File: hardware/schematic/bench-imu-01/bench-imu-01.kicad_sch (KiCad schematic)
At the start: 23 parts, among them J1 USB4105-GH-A, J2 UART, J3 SWD, SW1 SW_PUSH, U1 STM32G031K8T6, U2 BMI270, U3 TLV75533PDBV, U4 USBLC6-2SC6

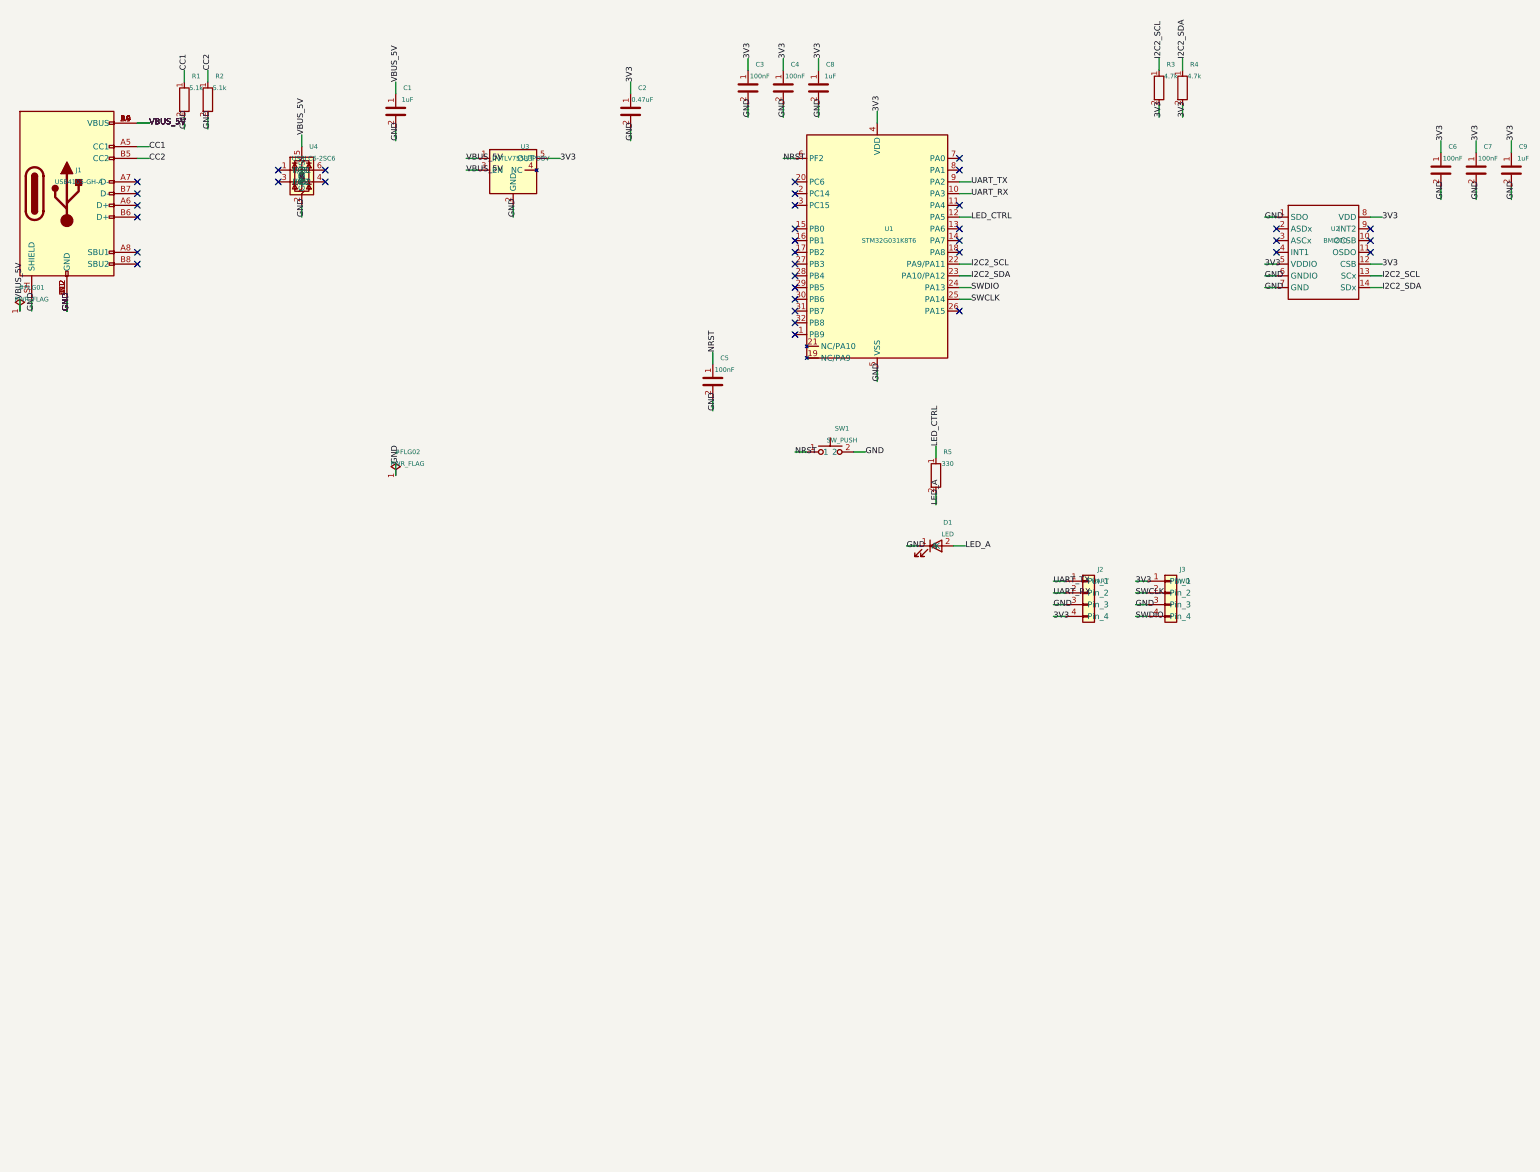
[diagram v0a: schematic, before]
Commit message: PCB Engineer: extend KiCad schematic to Rev 3-5 motor subsystem
The real KiCad project only ever captured Rev 2 (corrected) -- the
Motor Driver + Reaction Wheel subsystem (bench-imu-01-design.md section
7.5, already human-approved via bom/component-selection.md) was fully
designed but never transcribed into the actual .kicad_sch. Extends
generate_schematic.py (the project's own established authoring method)
to add all 25 new symbols: U5 (DRV10983, custom symbol, 24-pin HTSSOP,
pins independently re-verified against TI's real primary datasheet this
session), U6 (TPS26631PWPR, real library symbol+footprint), J4 (Same Sky
PJ-102AH barrel jack), D2/D3 (protection diodes), F1 (PTC fuse, custom
footprint -- no library match exists), R6-R15, C10-C17, and a new 3-pin
interconnect for M1 (motor is off-board; design doc section 10 itself
left this connector choice unresolved).

Every net wired exactly per the design doc's own net-by-net table
(re-derived into real distinct electrical nets, since that table
describes signal paths through series elements, not flat net
membership). Footprint decisions (CONFIRMED vs. ASSUMPTION, with
reasoning) recorded in hardware/schematic/bench-imu-01/README.md,
including a real power-rating-driven choice (R9 = 1206, not 0603, for
its stated 1/4W rating) and a disclosed, low-blast-radius open item
(J4's exact sleeve/switch/tip pin mapping -- primary datasheet diagram
not renderable by available tooling; D2's series reverse-polarity
protection fails safe if wrong).

Verified via kicad-cli sch erc + sch export netlist + sch export bom
(the established workaround for the broken kicad-* MCP tools, re-verified
still broken this session): 48 real components, zero ERC errors, 2
disclosed non-blocking warnings (one pre-existing from Rev 2, one new
metadata-completeness-only finding on U1 pin 19/PA9 -- kiutils 1.4.8
doesn't expose KiCad's per-instance 'alternate pin function' feature;
the wiring itself is electrically correct, independently re-confirme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
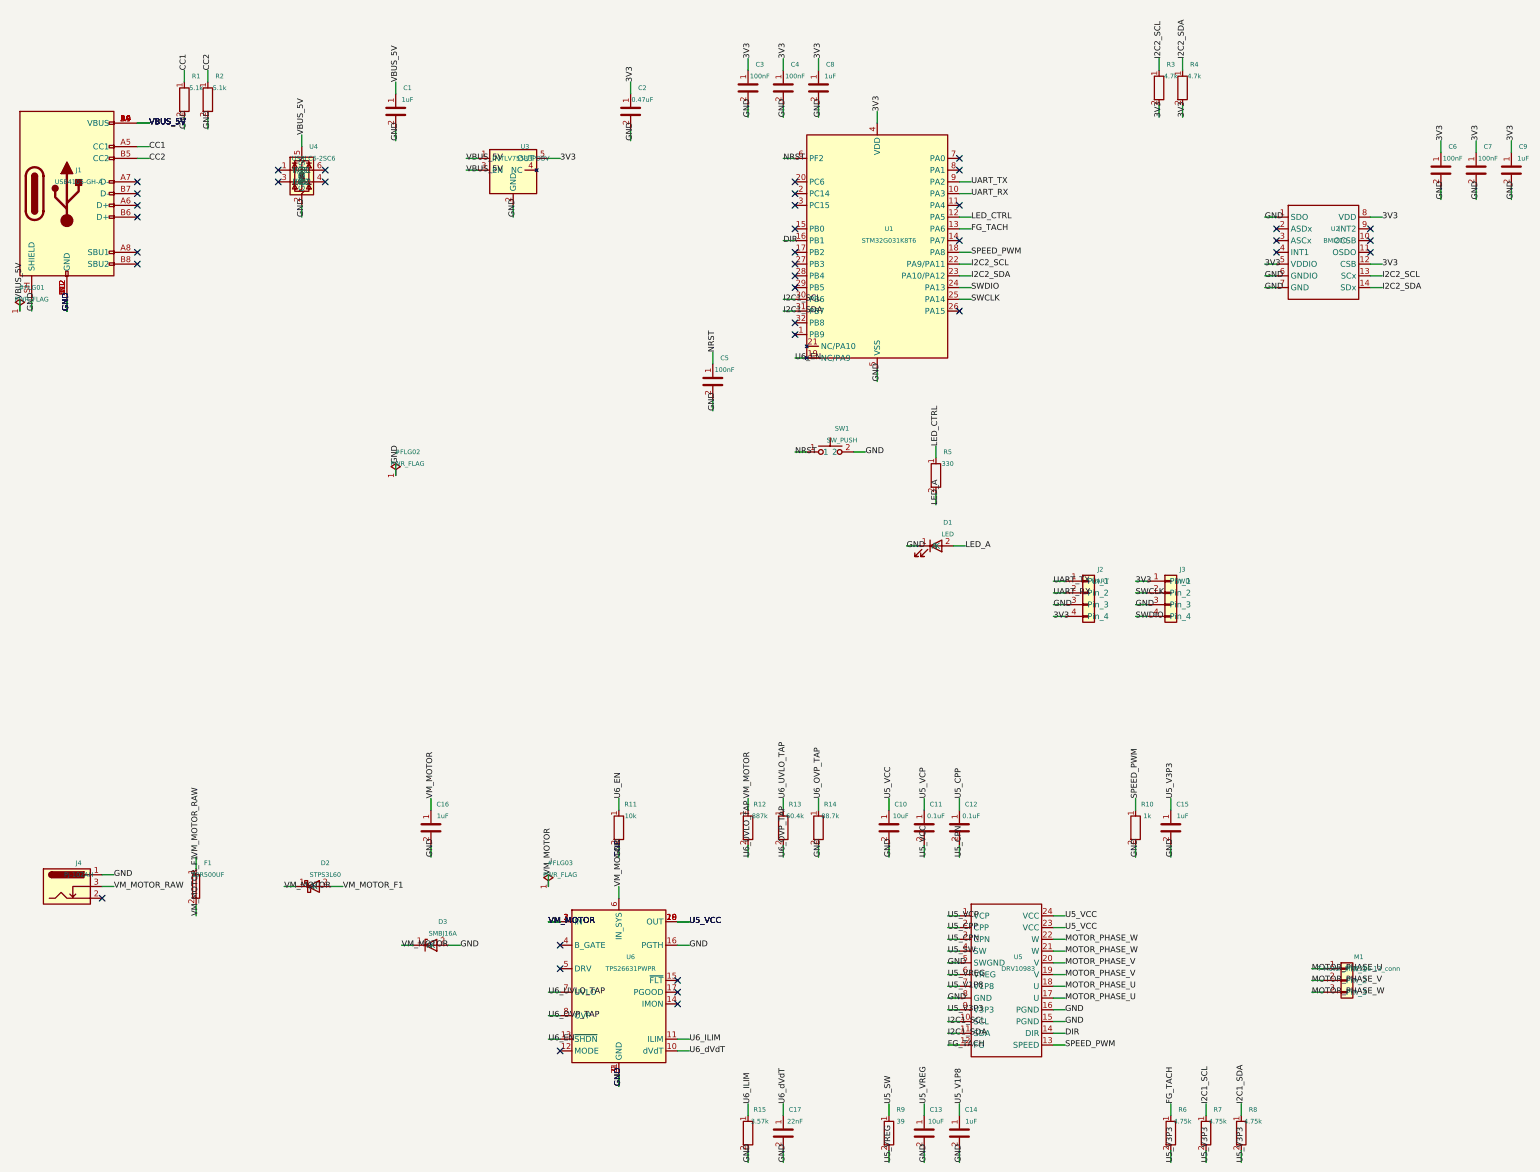
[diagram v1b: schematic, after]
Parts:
- added C10, C13: 10uF, Capacitor_SMD:C_0805_2012Metric, symbol Device:C
- added C11, C12: 0.1uF, Capacitor_SMD:C_0603_1608Metric, symbol Device:C
- added C14, C15, C16: 1uF, Capacitor_SMD:C_0603_1608Metric, symbol Device:C
- added C17: 22nF, Capacitor_SMD:C_0603_1608Metric, symbol Device:C
- added D2: STPS3L60, Diode_SMD:D_SMB, symbol Device:D_Schottky
- added D3: SMBJ16A, Diode_SMD:D_SMB, symbol Device:D_Zener
- added F1: 30R500UF, bench-imu-01:Fuse_Littelfuse_30R500UF_Radial_D14.0mm_P10.2mm, symbol Device:Fuse
- added J4: PJ-102AH, Connector_BarrelJack:BarrelJack_CUI_PJ-102AH_Horizontal, symbol Connector:Barrel_Jack_Switch
- added M1: T-Motor_MN2206-13_conn, TerminalBlock:TerminalBlock_MaiXu_MX126-5.0-03P_1x03_P5.00mm, symbol Connector_Generic:Conn_01x03
- added R10: 1k, Resistor_SMD:R_0603_1608Metric, symbol Device:R
- added R11: 10k, Resistor_SMD:R_0603_1608Metric, symbol Device:R
- added R12: 887k, Resistor_SMD:R_0603_1608Metric, symbol Device:R
- added R13: 60.4k, Resistor_SMD:R_0603_1608Metric, symbol Device:R
- added R14: 88.7k, Resistor_SMD:R_0603_1608Metric, symbol Device:R
- added R15: 3.57k, Resistor_SMD:R_0603_1608Metric, symbol Device:R
- added R6, R7, R8: 4.75k, Resistor_SMD:R_0603_1608Metric, symbol Device:R
- added R9: 39, Resistor_SMD:R_1206_3216Metric, symbol Device:R
- added U5: DRV10983, Package_SO:HTSSOP-24-1EP_4.4x7.8mm_P0.65mm_EP3.2x5mm, symbol bench-imu-01:DRV10983
- added U6: TPS26631PWPR, Package_SO:HTSSOP-20-1EP_4.4x6.5mm_P0.65mm_EP3.4x6.5mm_Mask2.96x2.96mm_ThermalVias, symbol Power_Management:TPS26631PWP
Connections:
- net GND: now also C10.2, C13.2, C14.2, C15.2, C16.2, C17.2, D3.2 (A), J4.1, R10.2, R11.2, R14.2, R15.2, U5.15 (PGND), U5.16 (PGND), U5.5 (SWGND), U5.8 (GND), U6.16 (PGTH), U6.21 (GND), U6.9 (GND)
- net FG_TACH: now reaches U1.13 (PA6)
- net FG_TACH: now also R6.1, U5.12 (FG)
- net DIR: now reaches U1.16 (PB1)
- net DIR: now also U5.14 (DIR)
- net SPEED_PWM: now reaches U1.18 (PA8)
- net SPEED_PWM: now also R10.1, U5.13 (SPEED)
- net U6_EN: now reaches U1.19 (NC/PA9)
- net U6_EN: now also R11.1, U6.13 (~{SHDN})
- net I2C1_SCL: now reaches U1.30 (PB6)
- net I2C1_SCL: now also R7.1, U5.10 (SCL)
- net I2C1_SDA: now reaches U1.31 (PB7)
- net I2C1_SDA: now also R8.1, U5.11 (SDA)
- new net MOTOR_PHASE_U: M1.1 (Pin_1), U5.17 (U), U5.18 (U)
- new net MOTOR_PHASE_V: M1.2 (Pin_2), U5.19 (V), U5.20 (V)
- new net MOTOR_PHASE_W: M1.3 (Pin_3), U5.21 (W), U5.22 (W)
- new net U5_CPN: C12.2, U5.3 (CPN)
- new net U5_CPP: C12.1, U5.2 (CPP)
- new net U5_SW: R9.1, U5.4 (SW)
- new net U5_V1P8: C14.1, U5.7 (V1P8)
- new net U5_V3P3: C15.1, R6.2, R7.2, R8.2, U5.9 (V3P3)
- new net U5_VCC: C10.1, C11.2, U5.23 (VCC), U5.24 (VCC), U6.18 (OUT), U6.19 (OUT), U6.20 (OUT)
- new net U5_VCP: C11.1, U5.1 (VCP)
- new net U5_VREG: C13.1, R9.2, U5.6 (VREG)
- new net U6_ILIM: R15.1, U6.11 (ILIM)
- new net U6_OVP_TAP: R13.2, R14.1, U6.8 (OVP)
- new net U6_UVLO_TAP: R12.2, R13.1, U6.7 (UVLO)
- new net U6_dVdT: C17.1, U6.10 (dVdT)
- new net VM_MOTOR: C16.1, D2.1 (K), D3.1 (K), R12.1, U6.1 (IN), U6.2 (IN), U6.3 (IN), U6.6 (IN_SYS)
- new net VM_MOTOR_F1: D2.2 (A), F1.2
- new net VM_MOTOR_RAW: F1.1, J4.3
- no-connect marks 36 -> 38

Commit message: PCB Engineer: fix ISS-030 (CRITICAL), ISS-033/034/035 (HIGH/MEDIUM), partial ISS-031 (HIGH)
Post-Hardware-Reviewer-Cycle-6 fix round. Fixes real bugs the independent
review found in the Rev 3-5 motor-subsystem schematic transcription and
first PCB layout (validation/design-review.md, commit 84db343).

ISS-030 (CRITICAL, RESOLVED): U1 pin 19 (PA9) was never actually a member
of the /U6_EN net despite a wire being drawn to it -- the shared
MCU_ST_STM32G0 library symbol declares pin 19's base electrical type as
no_connect, with PA9 only reachable via KiCad's per-instance "alternate
pin function" mechanism, which kiutils 1.4.8 cannot express. Fixed with a
patch_alternate_pin_function() post-processing step in
generate_schematic.py that injects (alternate "PA9") inside the
(pin "19" ...) s-expression directly in the raw .kicad_sch text (inserting
it as a sibling line instead breaks the file -- caught via kicad-cli sch
erc failing to parse during development of the fix). Verified via ERC
(0 errors, only the 1 pre-existing benign U3 lib_symbol_mismatch warning
remains) and kicad-cli sch export netlist (U1 pin 19 now confirmed a
genuine member of /U6_EN).

ISS-033/034/035 (HIGH/HIGH/MEDIUM, RESOLVED): generate_pcb.py's net
assignment used fp.FindPadByNumber(pin), which returns only the FIRST
physical pad when a footprint legitimately has several sharing one pad
number (U6's 17-sub-pad PowerPAD, J1's 4-pad USB shield, SW1's doubled
terminal pads) -- leaving every other same-numbered physical pad
genuinely unnetted, invisible to DRC's unconnected_items check. Fixed by
enumerating every matching physical pad and locally bridging them (a
same-number pad-to-pad track, independent of the later MST/Step-A routing
which only operates at (ref, pin) granularity). Independently
re-verified via a standalone pad/net audit script (not just re-trusting
the same DRC proxy that missed the bug originally): all of U6's 17
sub-pads, J1's 4 shield pads, and SW1's duplicate pads now share their
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
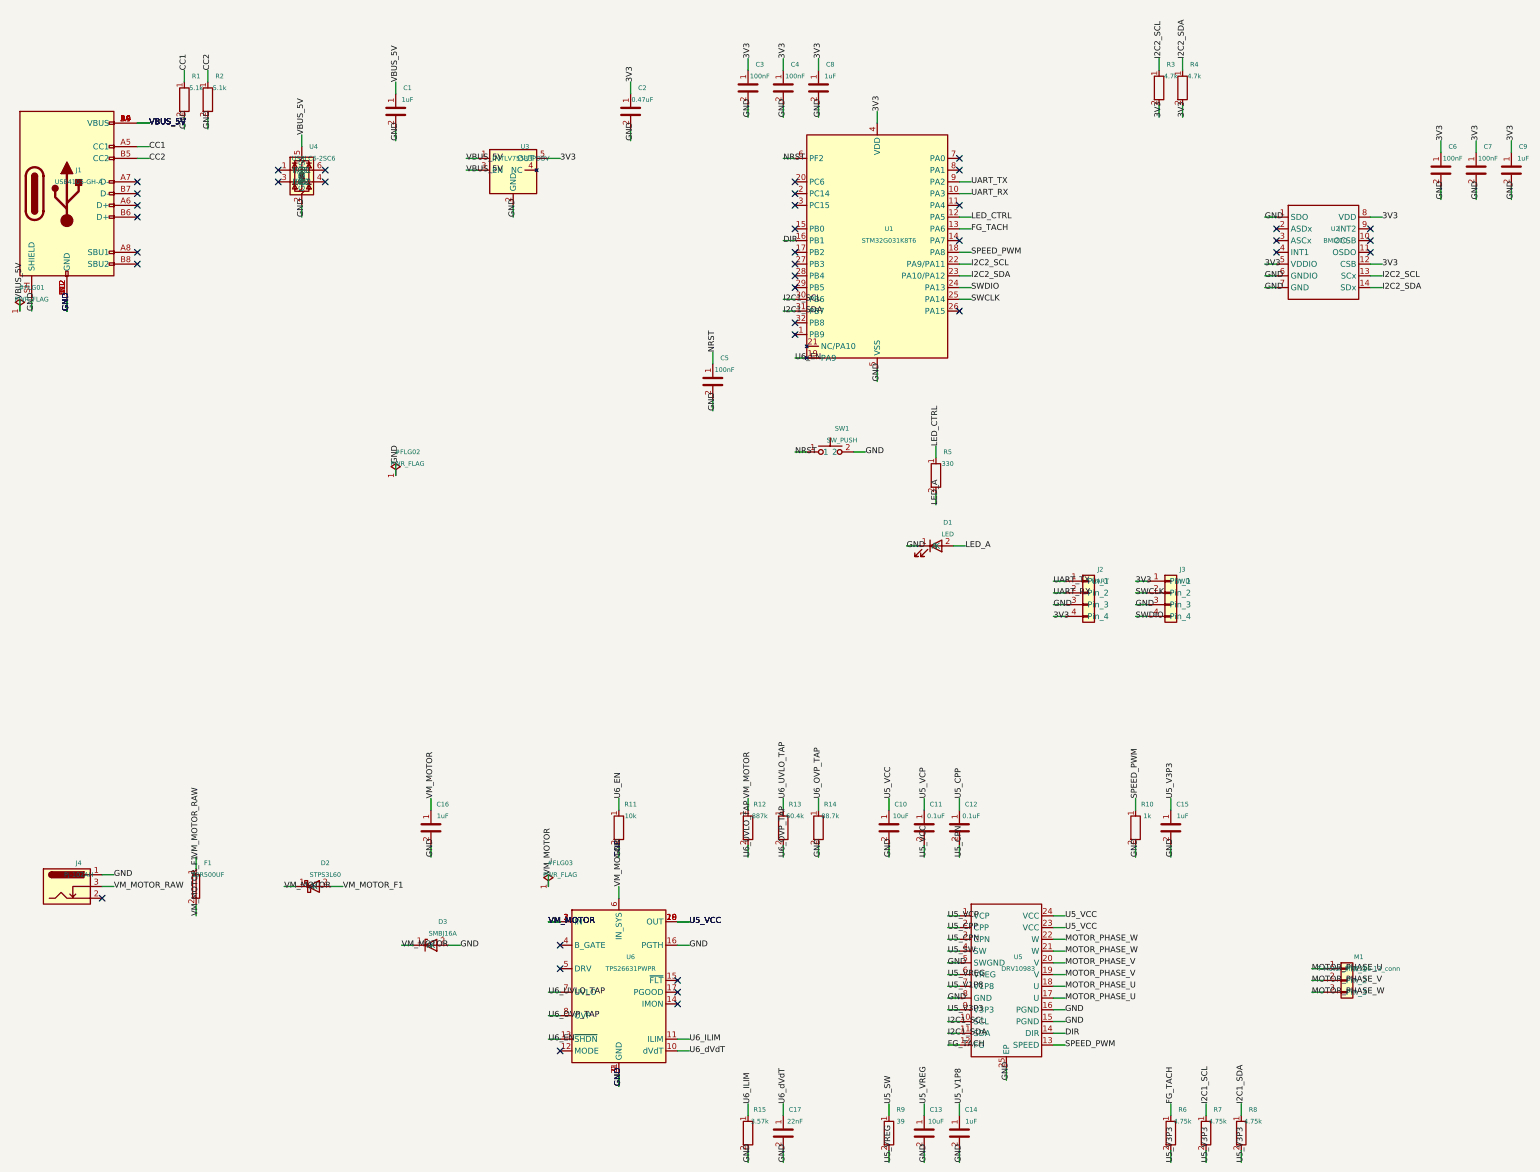
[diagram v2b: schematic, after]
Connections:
- net GND: now also U5.25 (EP)

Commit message: PCB Engineer: fix ISS-031 (HIGH) -- U5 thermal-via array, closing the last half
Continued iteration per Chief Engineer's disposition ("full authority to
keep going here"). Closes the second half of ISS-031 -- the first half
(pin 25/EP missing from the schematic symbol) was already fixed in an
earlier round; this fixes the footprint's lack of a thermal-via array.

Re-read DRV10983's own primary datasheet (SLVSCP6H) this cycle via the
same r.jina.ai text-extraction proxy already used elsewhere in this
project's history, specifically for its Layout Guidelines section (not
previously cited under any Evidence ID): "The exposed thermal pad must be
electrically connected to the ground plane through soldering to PCB for
proper operation and connected to bottom side of PCB through vias for
better thermal spreading," and "Keep the thermal pad connection as large
as possible, both on the bottom side and top side. It should be one
piece of copper without any gaps." Logged as DS-MTR-081 in
datasheets/evidence-log.md -- this is the part's OWN stated requirement,
stronger evidence than the generic SLMA002/SLMA004 PowerPAD app-note
citation the finding originally relied on.

Switched U5's footprint from the prior ASSUMPTION-labeled bare-pad custom
footprint (Package_SO:HTSSOP-24-1EP_4.4x7.8mm_P0.65mm_EP3.2x5mm, no via
array at all) to a real, standard KiCad library footprint
(...EP3.4x7.8mm_Mask2.4x4.68mm_ThermalVias) with an 18-via thermal array
(0.3mm drill / 0.6mm pad, matching the "0.3-0.33mm" guidance the finding
itself cited) and a larger 3.4x7.8mm F.Cu land, better matching the
datasheet's own "as large as possible" directive. Chose a real, vetted
library part over hand-building a custom via array from scratch --
verified all 3 HTSSOP-24-1EP-with-ThermalVias variants in KiCad's library
share the same F.Cu land size and differ only in via/mask sizing; picked
the one whose via drill (0.3mm) most closely matches the cited guidance.

Independently re-verified before marking RESO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
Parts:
- U5: footprint Package_SO:HTSSOP-24-1EP_4.4x7.8mm_P0.65mm_EP3.2x5mm -> Package_SO:HTSSOP-24-1EP_4.4x7.8mm_P0.65mm_EP3.4x7.8mm_Mask2.4x4.68mm_ThermalVias
